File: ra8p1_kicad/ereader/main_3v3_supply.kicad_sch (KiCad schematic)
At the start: 7 parts, among them U13 TPS63802DLAR

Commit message: Reconcile main-rail power budget with Octal NOR allocation
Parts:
- U13: Selection_Basis PWR-002/PWR-003; fixed PWM main digital converter; 1.65A al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 -> PWR-002/PWR-003; fixed PWM main digital converter; 1.80A al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
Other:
- note added: "PWR-003: LOAD, SOURCE AND STARTUP ACCEPTANCE LIMITS Main continuous allocation: 0.750 MCU + 0.500 radio + 0.250 SDRAM + 0.250 NOR + 0.050 logic = 1.800A. These are qualification allocations, not measured maximum currents. SD, camera, audio, display/touch/frontlight need separate SYS supplies. Pout=3.358485094*1.80=6.045273W. VIN>=3.20V allocation; raw trip min=3.263705831V. Allowed raw-to-VIN los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"
- note removed: "PWR-003: LOAD, SOURCE AND STARTUP ACCEPTANCE LIMITS Main continuous allocation: 0.750 MCU + 0.500 radio + 0.250 SDRAM + 0.100 NOR + 0.050 logic = 1.650A. These are qualification allocations, not measured maximum currents. SD, camera, audio, display/touch/frontlight need separate SYS supplies. Pout=3.358485094*1.65=5.541500W. VIN>=3.20V allocation; raw trip min=3.263705831V. Allowed raw-to-VIN los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"
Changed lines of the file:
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@@
 		(rev "0.3 DRAFT")
 	)
-	(text "PWR-003: LOAD, SOURCE AND STARTUP ACCEPTANCE LIMITS\nMain continuous allocation: 0.750 MCU + 0.500 radio\n+ 0.250 SDRAM + 0.100 NOR + 0.050 logic = 1.650A.\nThese are qualification allocations, not measured maximum currents.\nSD, camera, audio, display/touch/frontlight need separate SYS supplies.\n\nPout=3.358485094*1.65=5.541500W.\nVIN>=3.20V allocation; raw trip min=3.263705831V.\nAllowed raw-to-VIN loss=3.263705831-3.20=63.705831mV.\nAt ASSUMED eta=85%: Iin=Pout/(eta*3.20)=2.037316A.\nPloss=Pout*(1/eta-1)=0.977912W.\nReference rise=Ploss*81C/W=79.210859C; NOT enclosure prediction.\nVerify hot current capability and junction temperature <125C with margin.\n\nCold subtotal, RADIO OFF: 1.330 DCDC + 0.400 other = 1.730A.\nRadio on would give 2.230A > nominal 2A; keep radio OFF through start/wake.\nLargest wake-reference subtotal=1.270+0.400=1.670A.\nDCDC figures are reference-only; non-DCDC start and extra charging excluded.\nAdditional charging: I=Cadditional*dV/dt; qualify the actual ramp.\nTotal directly connected main-rail C <=1mF for SYS-007 discharge budget.\nNo externally driven +3V3_MCU: forced PWM can sink reverse current.\n\nPWR-002 static release margin: radio 14.922537mV; MCU 48.092861mV.\nRipple, startup and transients must fit; no fabrication release.\nFull sources, derivation and Python: ../design/power_decoupling.md PWR-003;\nsource-loss shutdown: ../design/system_power_design.md SYS-007."
+	(text "PWR-003: LOAD, SOURCE AND STARTUP ACCEPTANCE LIMITS\nMain continuous allocation: 0.750 MCU + 0.500 radio\n+ 0.250 SDRAM + 0.250 NOR + 0.050 logic = 1.800A.\nThese are qualification allocations, not measured maximum currents.\nSD, camera, audio, display/touch/frontlight need separate SYS supplies.\n\nPout=3.358485094*1.80=6.045273W.\nVIN>=3.20V allocation; raw trip min=3.263705831V.\nAllowed raw-to-VIN loss=3.263705831-3.20=63.705831mV.\nAt ASSUMED eta=85%: Iin=Pout/(eta*3.20)=2.222527A.\nPloss=Pout*(1/eta-1)=1.066813W.\nReference rise=Ploss*81C/W=86.411846C; NOT enclosure prediction.\nVerify hot current capability and junction temperature <125C with margin.\n\nCold subtotal, RADIO OFF: 1.330 DCDC + 0.550 other = 1.880A.\nRadio on would give 2.380A > nominal 2A; keep radio OFF through start/wake.\nLargest wake-reference subtotal=1.270+0.550=1.820A.\nDCDC figures are reference-only; non-DCDC start and extra charging excluded.\nAdditional charging: I=Cadditional*dV/dt; qualify the actual ramp.\nTotal directly connected main-rail C <=1mF for SYS-007 discharge budget.\nNo externally driven +3V3_MCU: forced PWM can sink reverse current.\n\nPWR-002 static release margin: radio 14.922537mV; MCU 48.092861mV.\nRipple, startup and transients must fit; no fabrication release.\nFull sources, derivation and Python: ../design/power_decoupling.md PWR-003;\nsource-loss shutdown: ../design/system_power_design.md SYS-007."
 		(exclude_from_sim no)
 		(at 215.646 139.7 0)
@@
 			)
 		)
-		(property "Selection_Basis" "PWR-002/PWR-003; fixed PWM main digital converter; 1.65A allocation; qualify startup, transient and thermal corners"
+		(property "Selection_Basis" "PWR-002/PWR-003; fixed PWM main digital converter; 1.80A allocation; qualify startup, transient and thermal corners"
 			(at 165.1 88.9 0)
 			(hide yes)

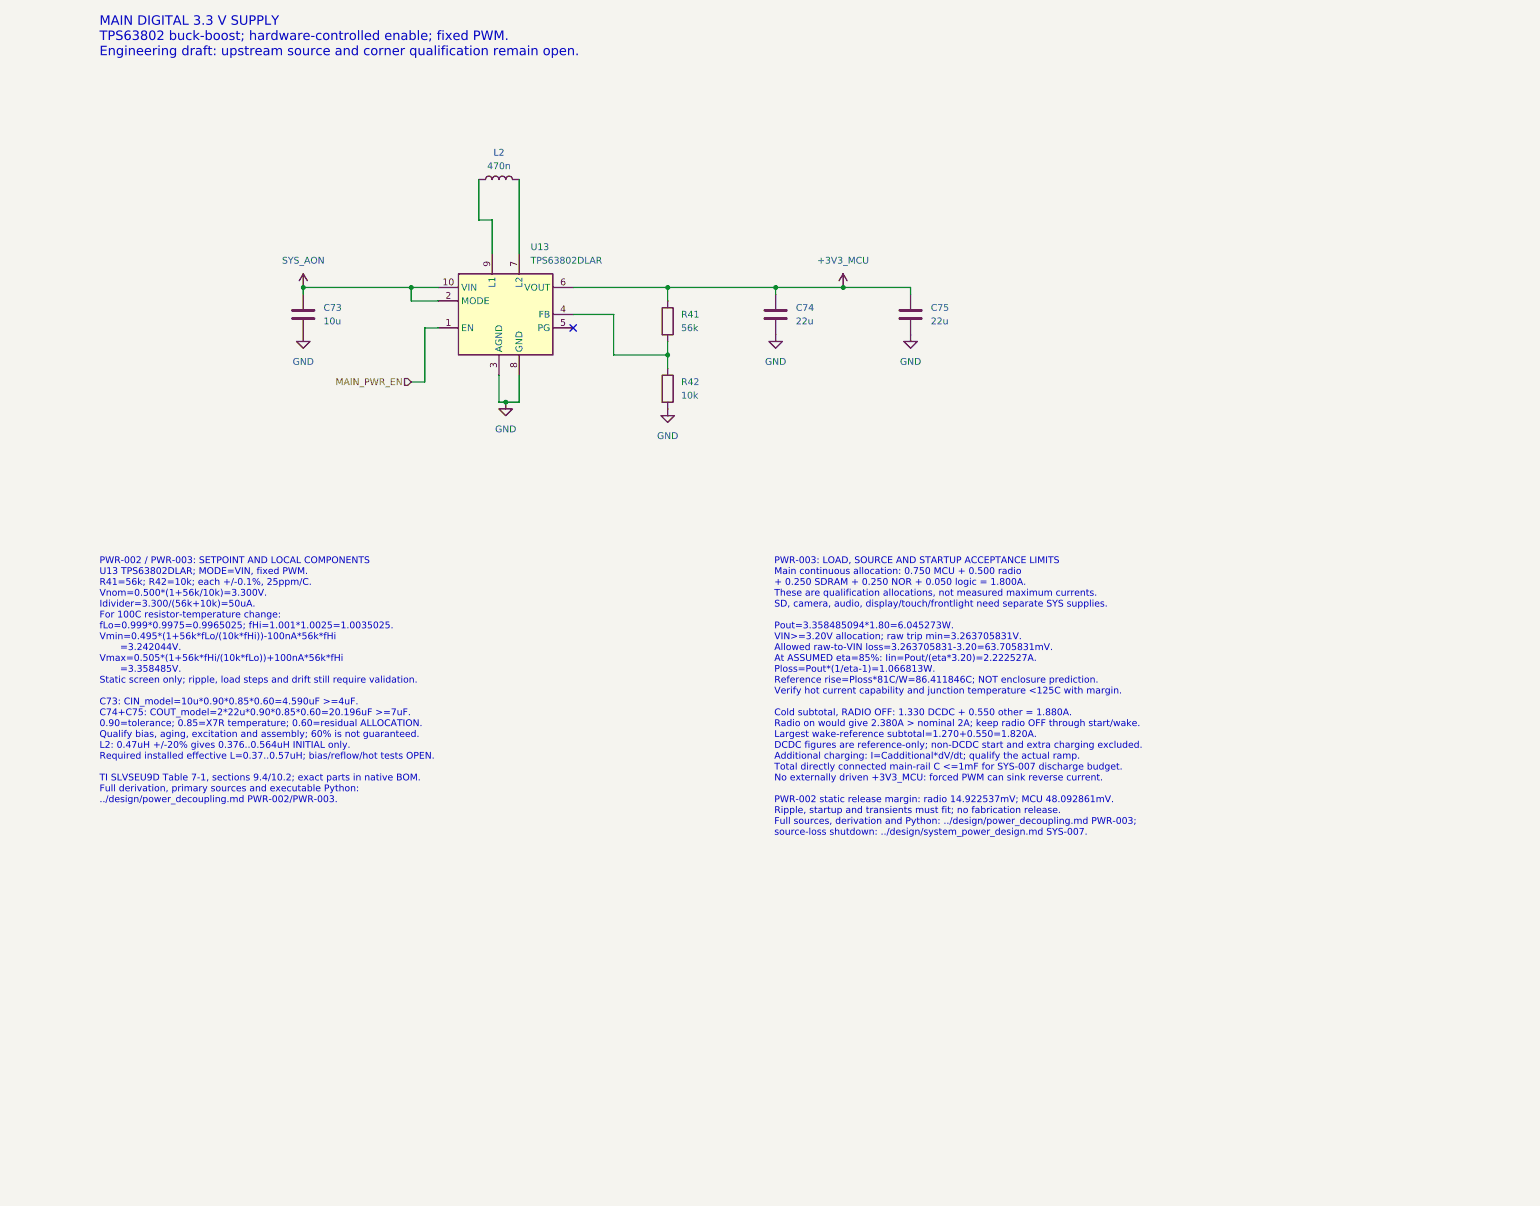
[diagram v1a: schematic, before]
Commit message: Wire LTC3119 power-stage draft and held RUN control
Add native RUN buffer and held-domain clamp with verified connectivity, sourced BOM fields, and linked PWR-004 calculations. Export the full schematic PDF and native BOM.

Keep rail adoption blocked by SDRAM logic-high conflict #846. Whole-project ERC remains 133 errors and two warnings; this checkpoint adds no findings.
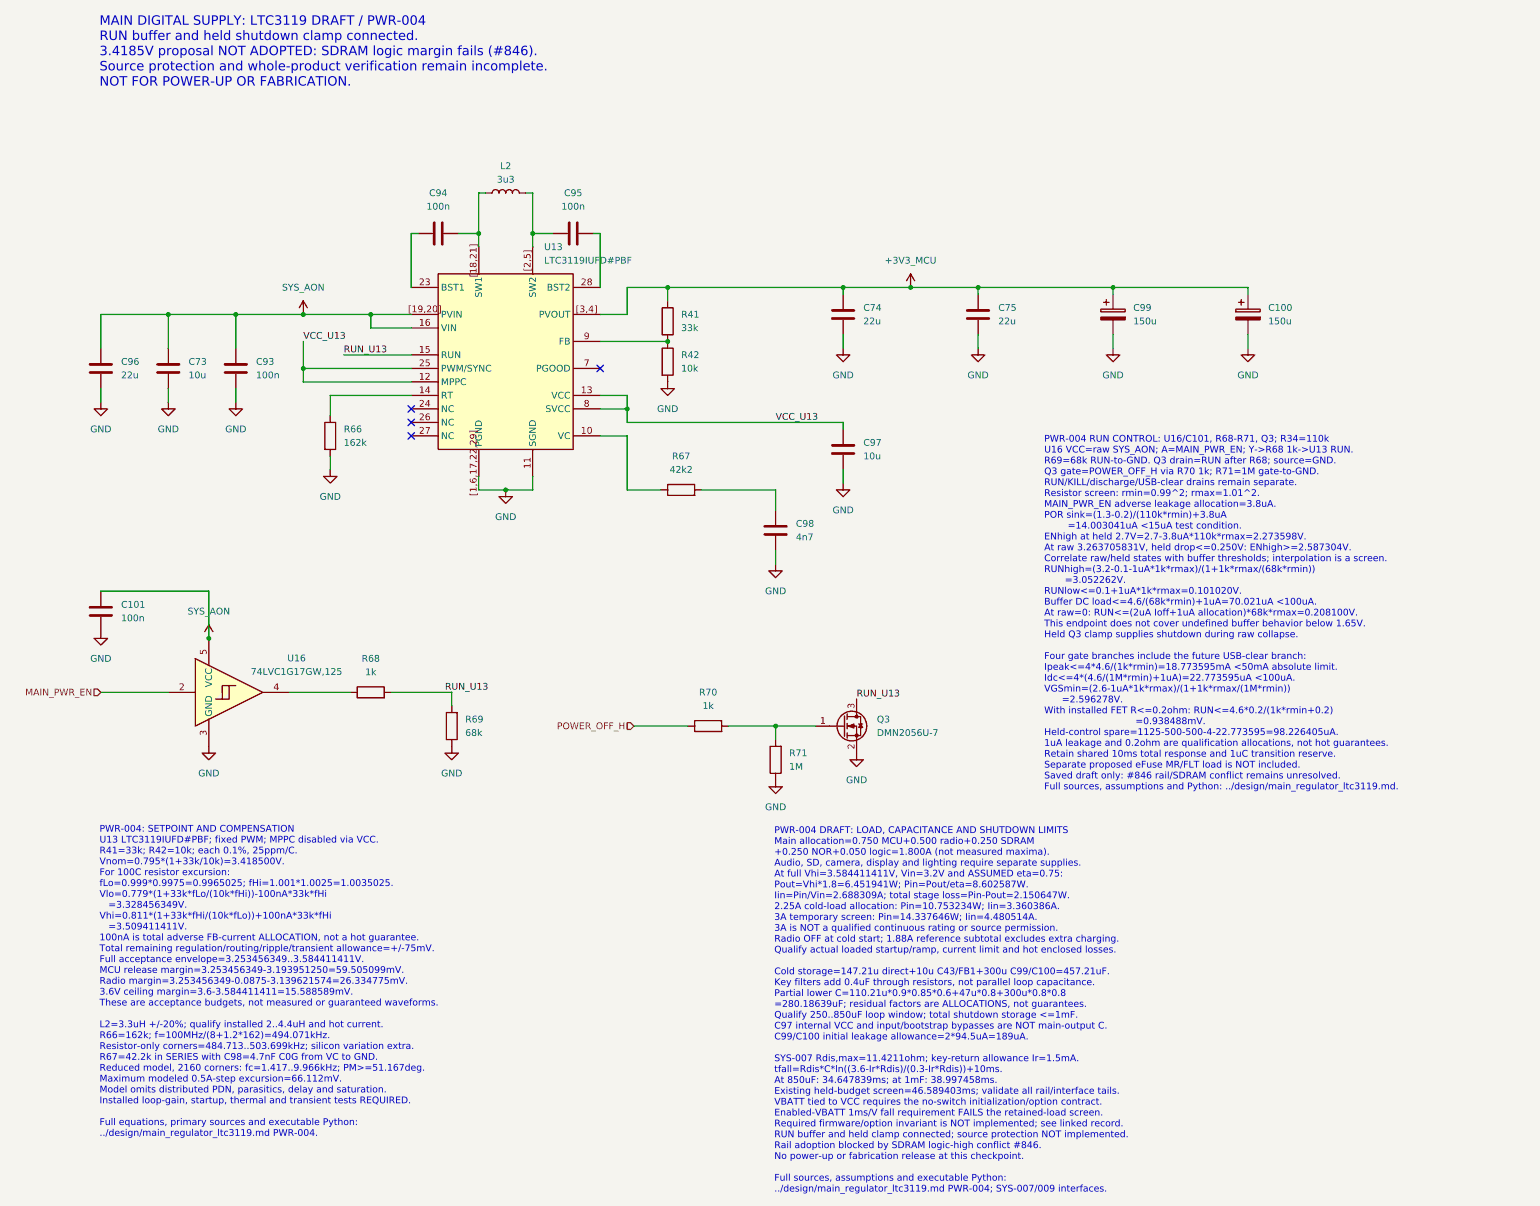
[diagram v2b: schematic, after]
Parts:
- added C100, C99: 150u, symbol Device:C_Polarized
- added C101, C93, C94, C95: 100n, symbol Device:C
- added C96: 22u, symbol Device:C
- added C97: 10u, symbol Device:C
- added C98: 4n7, symbol Device:C
- added Q3: DMN2056U-7, Package_TO_SOT_SMD:SOT-23, symbol Transistor_FET:DMN2056U
- added R66: 162k, symbol Device:R
- added R67: 42k2, symbol Device:R
- added R68, R70: 1k, symbol Device:R
- added R69: 68k, symbol Device:R
- added R71: 1M, symbol Device:R
- added U16: 74LVC1G17GW,125, symbol 74xGxx:74LVC1G17
- C73: Selection_Basis PWR-003; 10uF 35V X7R 10%; qualify >=4uF installed effectiv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 -> PWR-004: retained local 10uF PVIN input bypass in parallel 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
- C74, C75: Selection_Basis PWR-003; two 22uF 16V X7R 10% output capacitors; qualify >=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 -> PWR-004: one of two retained 22uF 16V X7R 10% output cerami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
- L2: value 470n -> 3u3; DigiKey_Part_Number 490-DFE322520F-R47M=P2CT-ND -> 283-EXLA1V0703-3R3-RCT-ND; DigiKey_URL https://www.digikey.com/en/products/detail/murata-electroni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 -> https://www.digikey.com/en/products/detail/eaton-electronic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; Manufacturer_Name Murata Electronics -> Eaton; Manufacturer_Part_Number DFE322520F-R47M=P2 -> EXLA1V0703-3R3-R; Procurement_Status Sourced candidate; electrical qualification pending; footpr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 -> Sourced candidate; installed electrical and thermal qualifi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; Selection_Basis PWR-003; 0.47uH candidate; qualify effective 0.37..0.57uH i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 -> PWR-004: 3.3uH +/-20%; 18mOhm max at 25C; 10A heating and 1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; Sourcing_Snapshot 2026-09-08; DigiKey stock 10298; USD qty1 0.58000; qty10 0.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 -> 2026-09-08; DigiKey stock 1393; USD qty1 1.44; qty10 1.182;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
- R41: value 56k -> 33k; DigiKey_Part_Number 408-1685-1-ND -> RG16P33.0KBCT-ND; DigiKey_URL https://www.digikey.com/en/products/detail/susumu/RG1608P-5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 -> https://www.digikey.com/en/products/detail/susumu/RG1608P-3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; Manufacturer_Part_Number RG1608P-563-B-T5 -> RG1608P-333-B-T5; Selection_Basis PWR-002/PWR-003; upper feedback 56k 0.1% 25ppm/C; 100C resi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 -> PWR-004: upper feedback 33k 0.1% 25ppm/C; 100C excursion an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; Sourcing_Snapshot 2026-09-08; DigiKey stock 40823; USD qty1 0.12000; qty10 0.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 -> 2026-09-08; DigiKey stock 18305; USD qty1 0.11; unreserved
- R42: Selection_Basis PWR-002/PWR-003; lower feedback 10k 0.1% 25ppm/C; 100C resi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 -> PWR-004: lower feedback 10k 0.1% 25ppm/C to quiet GND, pair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
- U13: value TPS63802DLAR -> LTC3119IUFD#PBF; symbol Power_Devices:TPS63802DLA -> Power_Devices:LTC3119IUFD#PBF; DigiKey_Part_Number 296-TPS63802DLARCT-ND -> 505-LTC3119IUFD#PBF-ND; DigiKey_URL https://www.digikey.com/en/products/detail/texas-instrument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 -> https://www.digikey.com/en/products/detail/analog-devices-i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; Manufacturer_Name Texas Instruments -> Analog Devices; Manufacturer_Part_Number TPS63802DLAR -> LTC3119IUFD#PBF; Procurement_Status Sourced candidate; electrical qualification pending; footpr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 -> Candidate - circuit integration and thermal/startup/loop qu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; Selection_Basis PWR-002/PWR-003; fixed PWM main digital converter; 1.80A al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 -> ADI 3119fb Rev B pp2,11-13: exact QFN pin map; visible nati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; Sourcing_Snapshot 2026-09-08; DigiKey stock 14665; USD qty1 2.83000; qty10 2.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 -> 2026-09-08 DigiKey stock 7024; Active; tube; USD1:24.07,10: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
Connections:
- net +3V3_MCU: now also U13.[3,4] (PVOUT), C100.1, C99.1; no longer U13.6 (VOUT)
- net GND: now also U13.11 (SGND), U13.[1,6,17,22,29] (PGND), C100.2, C101.2, C93.2, C96.2, C97.2, C98.2, C99.2, Q3.2 (S), R66.2, R69.1, R71.1, U16.3 (GND); no longer U13.3 (AGND), U13.8 (GND)
- net MAIN_PWR_EN: now also U16.2; no longer U13.1 (EN)
- net SYS_AON: now also U13.16 (VIN), U13.[19,20] (PVIN), C101.1, C93.1, C96.1, U16.5 (VCC); no longer U13.10 (VIN), U13.2 (MODE)
- net at R41.2, R42.1: now also U13.9 (FB); no longer U13.4 (FB)
- net at L2.2: now also U13.[2,5] (SW2), C95.1; no longer U13.7 (L2)
- net at L2.1: now also U13.[18,21] (SW1), C94.2; no longer U13.9 (L1)
- new net: Q3.1 (G), R70.2, R71.2
- new net: C98.1, R67.2
- new net: R66.1, U13.14 (RT)
- new net: C95.2, U13.28 (BST2)
- new net: R68.1, U16.4
- new net: R67.1, U13.10 (VC)
- new net: C94.1, U13.23 (BST1)
- new net POWER_OFF_H: R70.1
- new net RUN_U13: Q3.3 (D), R68.2, R69.2, U13.15 (RUN)
- new net VCC_U13: C97.1, U13.12 (MPPC), U13.13 (VCC), U13.25 (PWM/SYNC), U13.8 (SVCC)
- no-connect marks 1 -> 4
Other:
- note added: "MAIN DIGITAL SUPPLY: LTC3119 DRAFT / PWR-004 RUN buffer and held shutdown clamp connected. 3.4185V proposal NOT ADOPTED: SDRAM logic margin fails (#846). Source protection and whole-product verification remain incomplete. NOT FOR POWER-UP OR FABRICATION."
- note added: "PWR-004 DRAFT: LOAD, CAPACITANCE AND SHUTDOWN LIMITS Main allocation=0.750 MCU+0.500 radio+0.250 SDRAM +0.250 NOR+0.050 logic=1.800A (not measured maxima). Audio, SD, camera, display and lighting require separate supplies. At full Vhi=3.584411411V, Vin=3.2V and ASSUMED eta=0.75: Pout=Vhi*1.8=6.451941W; Pin=Pout/eta=8.602587W. Iin=Pin/Vin=2.688309A; total stage loss=Pin-Pout=2.150647W. 2.25A cold-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"
- note added: "PWR-004 RUN CONTROL: U16/C101, R68-R71, Q3; R34=110k U16 VCC=raw SYS_AON; A=MAIN_PWR_EN; Y->R68 1k->U13 RUN. R69=68k RUN-to-GND. Q3 drain=RUN after R68; source=GND. Q3 gate=POWER_OFF_H via R70 1k; R71=1M gate-to-GND. RUN/KILL/discharge/USB-clear drains remain separate. Resistor screen: rmin=0.99^2; rmax=1.01^2. MAIN_PWR_EN adverse leakage allocation=3.8uA. POR sink=(1.3-0.2)/(110k*rmin)+3.8uA =14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"
- note added: "PWR-004: SETPOINT AND COMPENSATION U13 LTC3119IUFD#PBF; fixed PWM; MPPC disabled via VCC. R41=33k; R42=10k; each 0.1%, 25ppm/C. Vnom=0.795*(1+33k/10k)=3.418500V. For 100C resistor excursion: fLo=0.999*0.9975=0.9965025; fHi=1.001*1.0025=1.0035025. Vlo=0.779*(1+33k*fLo/(10k*fHi))-100nA*33k*fHi =3.328456349V. Vhi=0.811*(1+33k*fHi/(10k*fLo))+100nA*33k*fHi =3.509411411V. 100nA is total adverse FB-curr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"
- note removed: "MAIN DIGITAL 3.3 V SUPPLY TPS63802 buck-boost; hardware-controlled enable; fixed PWM. Engineering draft: upstream source and corner qualification remain open."
- note removed: "PWR-002 / PWR-003: SETPOINT AND LOCAL COMPONENTS U13 TPS63802DLAR; MODE=VIN, fixed PWM. R41=56k; R42=10k; each +/-0.1%, 25ppm/C. Vnom=0.500*(1+56k/10k)=3.300V. Idivider=3.300/(56k+10k)=50uA. For 100C resistor-temperature change: fLo=0.999*0.9975=0.9965025; fHi=1.001*1.0025=1.0035025. Vmin=0.495*(1+56k*fLo/(10k*fHi))-100nA*56k*fHi =3.242044V. Vmax=0.505*(1+56k*fHi/(10k*fLo))+100nA*56k*fHi =3.35848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"
- note removed: "PWR-003: LOAD, SOURCE AND STARTUP ACCEPTANCE LIMITS Main continuous allocation: 0.750 MCU + 0.500 radio + 0.250 SDRAM + 0.250 NOR + 0.050 logic = 1.800A. These are qualification allocations, not measured maximum currents. SD, camera, audio, display/touch/frontlight need separate SYS supplies. Pout=3.358485094*1.80=6.045273W. VIN>=3.20V allocation; raw trip min=3.263705831V. Allowed raw-to-VIN los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"
- moved on the sheet: C73, C74, C75, L2, R42
